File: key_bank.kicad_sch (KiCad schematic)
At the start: 20 parts, among them IC2 ADG726BSUZ

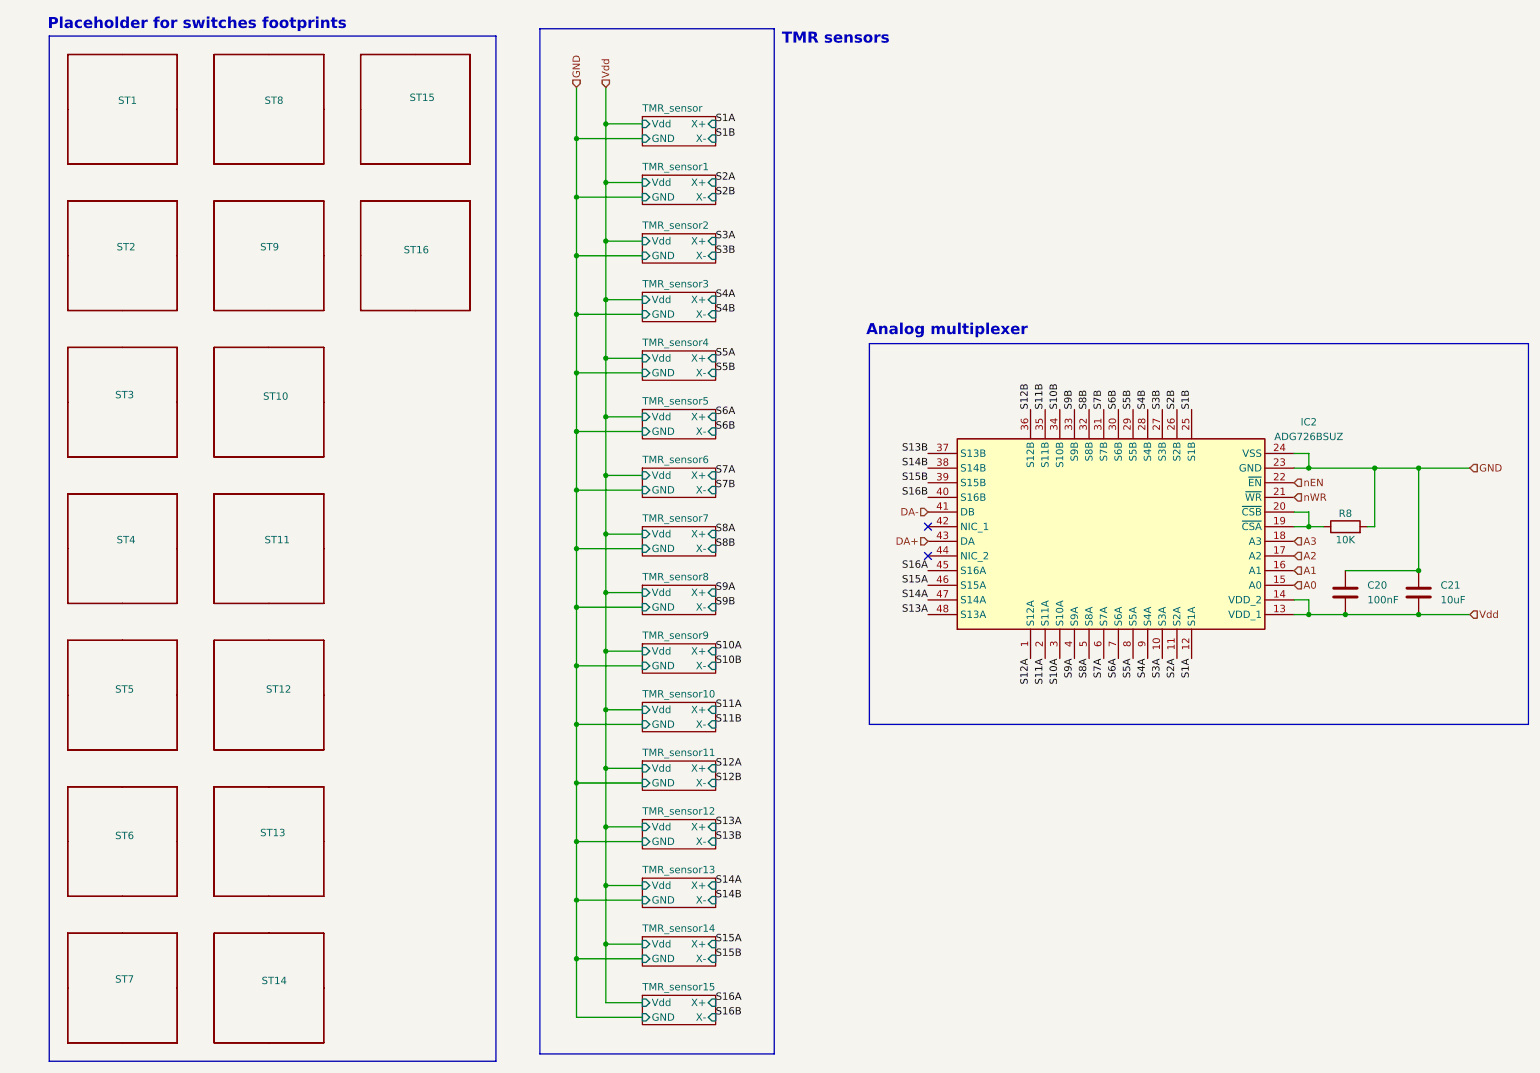
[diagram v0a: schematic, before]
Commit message: [UPDATE](PCB) placed LEDs
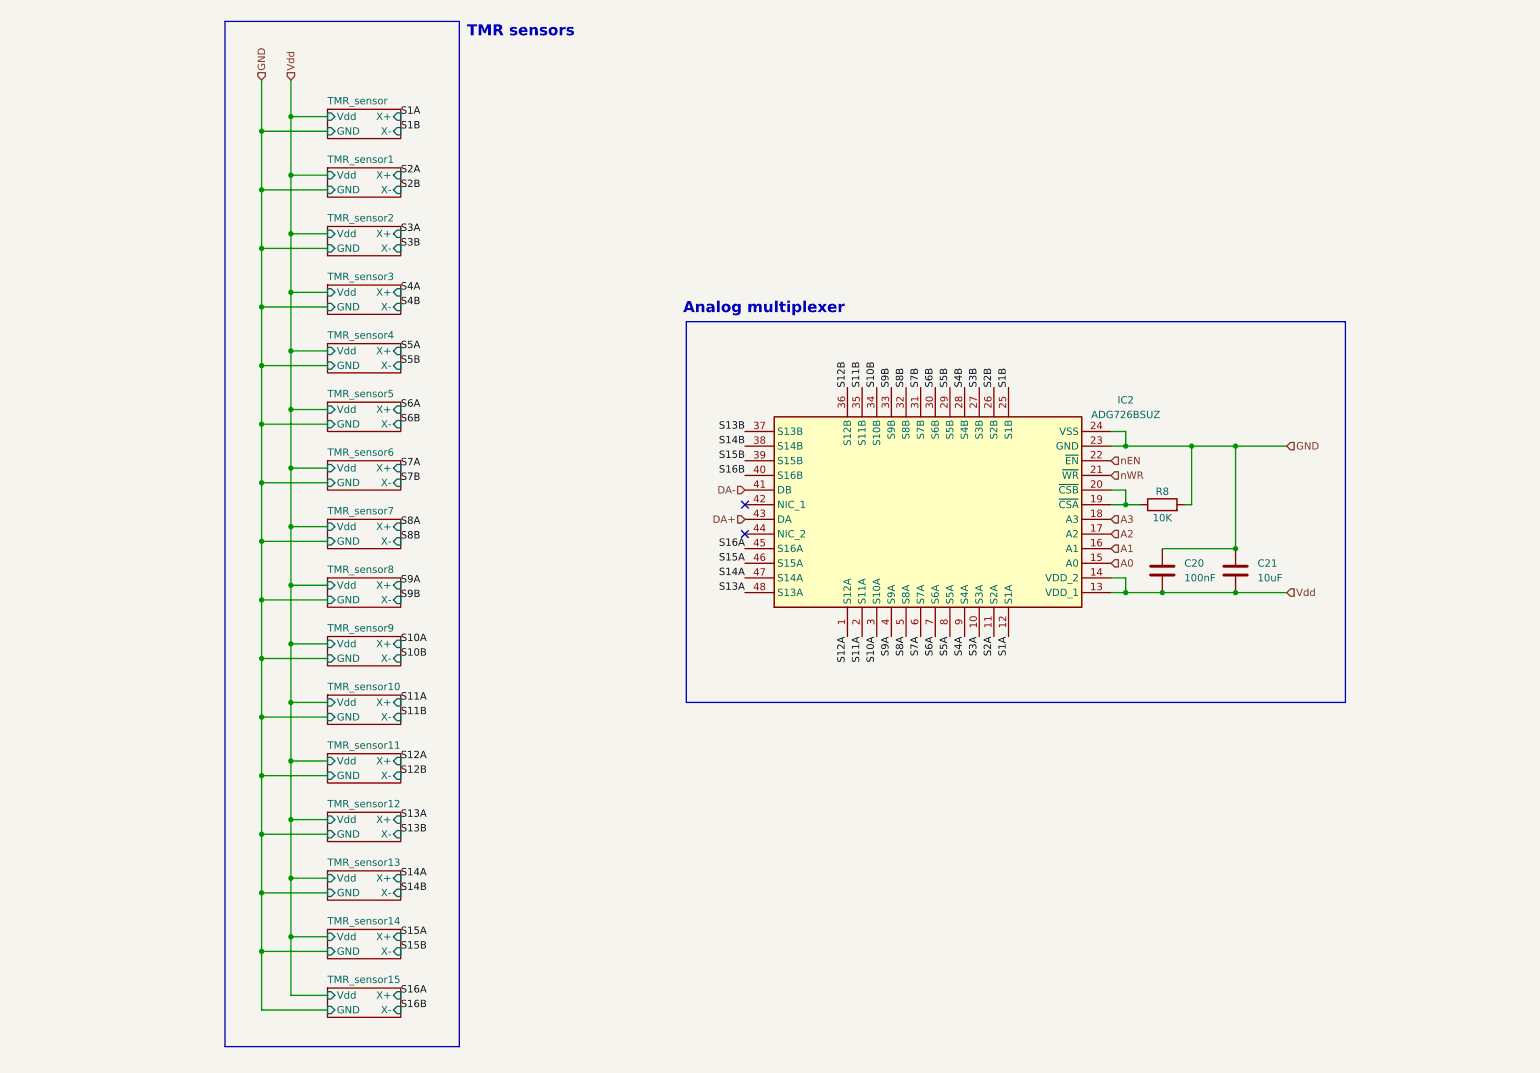
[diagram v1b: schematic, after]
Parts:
- removed ST1, ST10, ST11, ST12, ST13, ST14, ST15, ST16, ST2, ST3, ST4, ST5, ST6, ST7, ST8, ST9: ~, Switch_Keyboard_Cherry_MX:SW_Cherry_MX_PCB_Mag_1.00u, symbol switches:key_1
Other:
- note removed: "Placeholder for switches footprints"
- moved on the sheet: C20, C21, IC2, R8

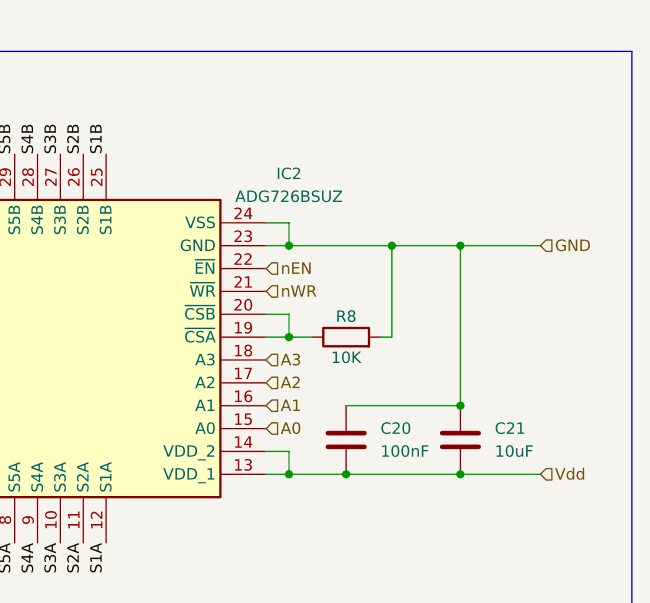
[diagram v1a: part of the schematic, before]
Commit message: [ADD](PCB) led and tmr caps placement
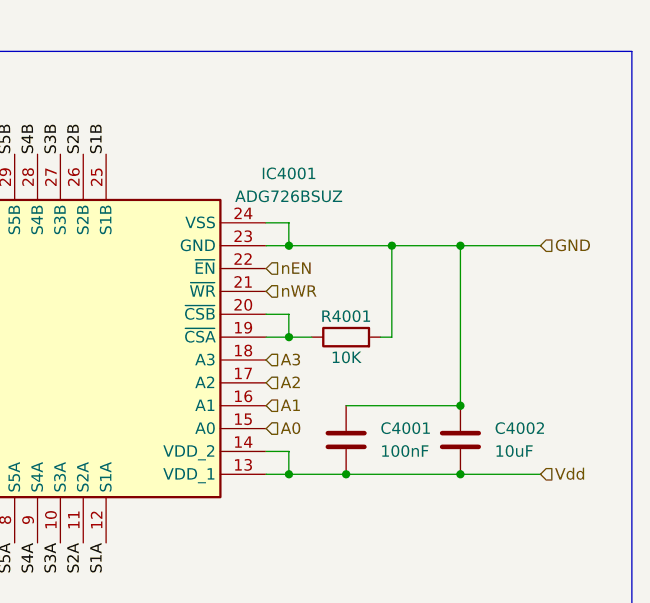
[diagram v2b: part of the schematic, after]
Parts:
- renumbered C20 to C4001, C21 to C4002, IC2 to IC4001, R8 to R4001
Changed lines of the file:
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@@
 		(dnp no)
 		(fields_autoplaced yes)
-		(property "Reference" "IC2"
+		(property "Reference" "IC4001"
 			(at 203.2 80.9146 90)
 			(effects
@@
 			(project "RyzzenKeyboard"
 				(path "/5d44d704-6136-40a8-98a4-93f001ea8743/c5dd3d76-8c7d-4253-bbc0-6b560edbfa92/3aabb479-c219-4268-aef4-9e1f740b8389"
-					(reference "IC4")
+					(reference "IC204001")
 					(unit 1)
 				)
 				(path "/5d44d704-6136-40a8-98a4-93f001ea8743/c5dd3d76-8c7d-4253-bbc0-6b560edbfa92/735f3a62-f16a-407d-b596-d90350aa3066"
-					(reference "IC2")
+					(reference "IC4001")
 					(unit 1)
 				)
@@
 		(on_board yes)
 		(dnp no)
-		(property "Reference" "R8"
+		(property "Reference" "R4001"
 			(at 209.55 96.774 90)
 			(effects
@@
 			(project "RyzzenKeyboard"
 				(path "/5d44d704-6136-40a8-98a4-93f001ea8743/c5dd3d76-8c7d-4253-bbc0-6b560edbfa92/3aabb479-c219-4268-aef4-9e1f740b8389"
-					(reference "R10")
+					(reference "R204001")
 					(unit 1)
 				)
 				(path "/5d44d704-6136-40a8-98a4-93f001ea8743/c5dd3d76-8c7d-4253-bbc0-6b560edbfa92/735f3a62-f16a-407d-b596-d90350aa3066"
-					(reference "R8")
+					(reference "R4001")
 					(unit 1)
 				)
@@
 		(dnp no)
 		(fields_autoplaced yes)
-		(property "Reference" "C21"
+		(property "Reference" "C4002"
 			(at 226.06 109.2199 0)
 			(effects
@@
 			(project "RyzzenKeyboard"
 				(path "/5d44d704-6136-40a8-98a4-93f001ea8743/c5dd3d76-8c7d-4253-bbc0-6b560edbfa92/3aabb479-c219-4268-aef4-9e1f740b8389"
-					(reference "C30")
+					(reference "C204002")
 					(unit 1)
 				)
 				(path "/5d44d704-6136-40a8-98a4-93f001ea8743/c5dd3d76-8c7d-4253-bbc0-6b560edbfa92/735f3a62-f16a-407d-b596-d90350aa3066"
-					(reference "C21")
+					(reference "C4002")
 					(unit 1)
 				)
@@
 		(dnp no)
 		(fields_autoplaced yes)
-		(property "Reference" "C20"
+		(property "Reference" "C4001"
 			(at 213.36 109.2199 0)
 			(effects
@@
 			(project "RyzzenKeyboard"
 				(path "/5d44d704-6136-40a8-98a4-93f001ea8743/c5dd3d76-8c7d-4253-bbc0-6b560edbfa92/3aabb479-c219-4268-aef4-9e1f740b8389"
-					(reference "C29")
+					(reference "C204001")
 					(unit 1)
 				)
 				(path "/5d44d704-6136-40a8-98a4-93f001ea8743/c5dd3d76-8c7d-4253-bbc0-6b560edbfa92/735f3a62-f16a-407d-b596-d90350aa3066"
-					(reference "C20")
+					(reference "C4001")
 					(unit 1)
 				)
@@
 				)
 				(path "/5d44d704-6136-40a8-98a4-93f001ea8743/c5dd3d76-8c7d-4253-bbc0-6b560edbfa92/3aabb479-c219-4268-aef4-9e1f740b8389"
-					(page "29")
+					(page "25")
 				)
 			)
@@
 			(project "RyzzenKeyboard"
 				(path "/5d44d704-6136-40a8-98a4-93f001ea8743/c5dd3d76-8c7d-4253-bbc0-6b560edbfa92/735f3a62-f16a-407d-b596-d90350aa3066"
-					(page "7")
-				)
-				(path "/5d44d704-6136-40a8-98a4-93f001ea8743/c5dd3d76-8c7d-4253-bbc0-6b560edbfa92/3aabb479-c219-4268-aef4-9e1f740b8389"
-					(page "20")
+					(page "8")
+				)
+				(path "/5d44d704-6136-40a8-98a4-93f001ea8743/c5dd3d76-8c7d-4253-bbc0-6b560edbfa92/3aabb479-c219-4268-aef4-9e1f740b8389"
+					(page "24")
 				)
 			)
@@
 			(project "RyzzenKeyboard"
 				(path "/5d44d704-6136-40a8-98a4-93f001ea8743/c5dd3d76-8c7d-4253-bbc0-6b560edbfa92/735f3a62-f16a-407d-b596-d90350aa3066"
-					(page "24")
-				)
-				(path "/5d44d704-6136-40a8-98a4-93f001ea8743/c5dd3d76-8c7d-4253-bbc0-6b560edbfa92/3aabb479-c219-4268-aef4-9e1f740b8389"
-					(page "35")
+					(page "18")
+				)
+				(path "/5d44d704-6136-40a8-98a4-93f001ea8743/c5dd3d76-8c7d-4253-bbc0-6b560edbfa92/3aabb479-c219-4268-aef4-9e1f740b8389"
+					(page "34")
 				)
 			)
@@
 			(project "RyzzenKeyboard"
 				(path "/5d44d704-6136-40a8-98a4-93f001ea8743/c5dd3d76-8c7d-4253-bbc0-6b560edbfa92/735f3a62-f16a-407d-b596-d90350aa3066"
-					(page "21")
-				)
-				(path "/5d44d704-6136-40a8-98a4-93f001ea8743/c5dd3d76-8c7d-4253-bbc0-6b560edbfa92/3aabb479-c219-4268-aef4-9e1f740b8389"
-					(page "32")
+					(page "15")
+				)
+				(path "/5d44d704-6136-40a8-98a4-93f001ea8743/c5dd3d76-8c7d-4253-bbc0-6b560edbfa92/3aabb479-c219-4268-aef4-9e1f740b8389"
+					(page "31")
 				)
 			)
@@
 			(project "RyzzenKeyboard"
 				(path "/5d44d704-6136-40a8-98a4-93f001ea8743/c5dd3d76-8c7d-4253-bbc0-6b560edbfa92/735f3a62-f16a-407d-b596-d90350aa3066"
-					(page "27")
-				)
-				(path "/5d44d704-6136-40a8-98a4-93f001ea8743/c5dd3d76-8c7d-4253-bbc0-6b560edbfa92/3aabb479-c219-4268-aef4-9e1f740b8389"
-					(page "38")
+					(page "21")
+				)
+				(path "/5d44d704-6136-40a8-98a4-93f001ea8743/c5dd3d76-8c7d-4253-bbc0-6b560edbfa92/3aabb479-c219-4268-aef4-9e1f740b8389"
+					(page "37")
 				)
 			)
@@
 			(project "RyzzenKeyboard"
 				(path "/5d44d704-6136-40a8-98a4-93f001ea8743/c5dd3d76-8c7d-4253-bbc0-6b560edbfa92/735f3a62-f16a-407d-b596-d90350aa3066"
-					(page "23")
-				)
-				(path "/5d44d704-6136-40a8-98a4-93f001ea8743/c5dd3d76-8c7d-4253-bbc0-6b560edbfa92/3aabb479-c219-4268-aef4-9e1f740b8389"
-					(page "34")
+					(page "17")
+				)
+				(path "/5d44d704-6136-40a8-98a4-93f001ea8743/c5dd3d76-8c7d-4253-bbc0-6b560edbfa92/3aabb479-c219-4268-aef4-9e1f740b8389"
+					(page "33")
 				)
 			)
@@
 			(project "RyzzenKeyboard"
 				(path "/5d44d704-6136-40a8-98a4-93f001ea8743/c5dd3d76-8c7d-4253-bbc0-6b560edbfa92/735f3a62-f16a-407d-b596-d90350aa3066"
-					(page "15")
-				)
-				(path "/5d44d704-6136-40a8-98a4-93f001ea8743/c5dd3d76-8c7d-4253-bbc0-6b560edbfa92/3aabb479-c219-4268-aef4-9e1f740b8389"
-					(page "18")
+					(page "13")
+				)
+				(path "/5d44d704-6136-40a8-98a4-93f001ea8743/c5dd3d76-8c7d-4253-bbc0-6b560edbfa92/3aabb479-c219-4268-aef4-9e1f740b8389"
+					(page "29")
 				)
 			)
@@
 			(project "RyzzenKeyboard"
 				(path "/5d44d704-6136-40a8-98a4-93f001ea8743/c5dd3d76-8c7d-4253-bbc0-6b560edbfa92/735f3a62-f16a-407d-b596-d90350aa3066"
-					(page "22")
-				)
-				(path "/5d44d704-6136-40a8-98a4-93f001ea8743/c5dd3d76-8c7d-4253-bbc0-6b560edbfa92/3aabb479-c219-4268-aef4-9e1f740b8389"
-					(page "30")
+					(page "16")
+				)
+				(path "/5d44d704-6136-40a8-98a4-93f001ea8743/c5dd3d76-8c7d-4253-bbc0-6b560edbfa92/3aabb479-c219-4268-aef4-9e1f740b8389"
+					(page "32")
 				)
 			)
@@
 			(project "RyzzenKeyboard"
 				(path "/5d44d704-6136-40a8-98a4-93f001ea8743/c5dd3d76-8c7d-4253-bbc0-6b560edbfa92/735f3a62-f16a-407d-b596-d90350aa3066"
-					(page "28")
-				)
-				(path "/5d44d704-6136-40a8-98a4-93f001ea8743/c5dd3d76-8c7d-4253-bbc0-6b560edbfa92/3aabb479-c219-4268-aef4-9e1f740b8389"
-					(page "39")
+					(page "22")
+				)
+				(path "/5d44d704-6136-40a8-98a4-93f001ea8743/c5dd3d76-8c7d-4253-bbc0-6b560edbfa92/3aabb479-c219-4268-aef4-9e1f740b8389"
+					(page "38")
 				)
 			)
@@
 			(project "RyzzenKeyboard"
 				(path "/5d44d704-6136-40a8-98a4-93f001ea8743/c5dd3d76-8c7d-4253-bbc0-6b560edbfa92/735f3a62-f16a-407d-b596-d90350aa3066"
-					(page "33")
-				)
-				(path "/5d44d704-6136-40a8-98a4-93f001ea8743/c5dd3d76-8c7d-4253-bbc0-6b560edbfa92/3aabb479-c219-4268-aef4-9e1f740b8389"
-					(page "19")
+					(page "7")
+				)
+				(path "/5d44d704-6136-40a8-98a4-93f001ea8743/c5dd3d76-8c7d-4253-bbc0-6b560edbfa92/3aabb479-c219-4268-aef4-9e1f740b8389"
+					(page "23")
 				)
 			)
@@
 			(project "RyzzenKeyboard"
 				(path "/5d44d704-6136-40a8-98a4-93f001ea8743/c5dd3d76-8c7d-4253-bbc0-6b560edbfa92/735f3a62-f16a-407d-b596-d90350aa3066"
-					(page "13")
-				)
-				(path "/5d44d704-6136-40a8-98a4-93f001ea8743/c5dd3d76-8c7d-4253-bbc0-6b560edbfa92/3aabb479-c219-4268-aef4-9e1f740b8389"
-					(page "17")
+					(page "11")
+				)
+				(path "/5d44d704-6136-40a8-98a4-93f001ea8743/c5dd3d76-8c7d-4253-bbc0-6b560edbfa92/3aabb479-c219-4268-aef4-9e1f740b8389"
+					(page "27")
 				)
 			)
@@
 			(project "RyzzenKeyboard"
 				(path "/5d44d704-6136-40a8-98a4-93f001ea8743/c5dd3d76-8c7d-4253-bbc0-6b560edbfa92/735f3a62-f16a-407d-b596-d90350aa3066"
-					(page "16")
-				)
-				(path "/5d44d704-6136-40a8-98a4-93f001ea8743/c5dd3d76-8c7d-4253-bbc0-6b560edbfa92/3aabb479-c219-4268-aef4-9e1f740b8389"
-					(page "31")
+					(page "14")
+				)
+				(path "/5d44d704-6136-40a8-98a4-93f001ea8743/c5dd3d76-8c7d-4253-bbc0-6b560edbfa92/3aabb479-c219-4268-aef4-9e1f740b8389"
+					(page "30")
 				)
 			)
@@
 			(project "RyzzenKeyboard"
 				(path "/5d44d704-6136-40a8-98a4-93f001ea8743/c5dd3d76-8c7d-4253-bbc0-6b560edbfa92/735f3a62-f16a-407d-b596-d90350aa3066"
-					(page "14")
-				)
-				(path "/5d44d704-6136-40a8-98a4-93f001ea8743/c5dd3d76-8c7d-4253-bbc0-6b560edbfa92/3aabb479-c219-4268-aef4-9e1f740b8389"
-					(page "11")
+					(page "12")
+				)
+				(path "/5d44d704-6136-40a8-98a4-93f001ea8743/c5dd3d76-8c7d-4253-bbc0-6b560edbfa92/3aabb479-c219-4268-aef4-9e1f740b8389"
+					(page "28")
 				)
 			)
@@
 			(project "RyzzenKeyboard"
 				(path "/5d44d704-6136-40a8-98a4-93f001ea8743/c5dd3d76-8c7d-4253-bbc0-6b560edbfa92/735f3a62-f16a-407d-b596-d90350aa3066"
-					(page "25")
-				)
-				(path "/5d44d704-6136-40a8-98a4-93f001ea8743/c5dd3d76-8c7d-4253-bbc0-6b560edbfa92/3aabb479-c219-4268-aef4-9e1f740b8389"
-					(page "37")
+					(page "19")
+				)
+				(path "/5d44d704-6136-40a8-98a4-93f001ea8743/c5dd3d76-8c7d-4253-bbc0-6b560edbfa92/3aabb479-c219-4268-aef4-9e1f740b8389"
+					(page "35")
 				)
 			)
@@
 				)
 				(path "/5d44d704-6136-40a8-98a4-93f001ea8743/c5dd3d76-8c7d-4253-bbc0-6b560edbfa92/3aabb479-c219-4268-aef4-9e1f740b8389"
-					(page "12")
+					(page "26")
 				)
 			)
@@
 			(project "RyzzenKeyboard"
 				(path "/5d44d704-6136-40a8-98a4-93f001ea8743/c5dd3d76-8c7d-4253-bbc0-6b560edbfa92/735f3a62-f16a-407d-b596-d90350aa3066"
-					(page "26")
-				)
-				(path "/5d44d704-6136-40a8-98a4-93f001ea8743/c5dd3d76-8c7d-4253-bbc0-6b560edbfa92/3aabb479-c219-4268-aef4-9e1f740b8389"
+					(page "20")
+				)
+				(path "/5d44d704-6136-40a8-98a4-93f001ea8743/c5dd3d76-8c7d-4253-bbc0-6b560edbfa92/3aabb479-c219-4268-aef4-9e1f740b8389"
